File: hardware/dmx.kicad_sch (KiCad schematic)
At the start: 38 parts, among them J101 Cortex, J102 DX07S016JA3, SW101 SKSG, SW102 SKSG, U101 TPS78433QWDRBRQ1, U102 ATSAMD51G, Y101 32k768

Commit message: Update Library
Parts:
- C101: symbol V2_Device:C_0603_10u -> V2_Capacitor:0603_10u
- C102, C103, C104, C105: symbol V2_Device:C_0603_0u1 -> V2_Capacitor:0603_0u1
- C106, C107: symbol V2_Device:C_0805_10u -> V2_Capacitor:0805_10u
- C108, C109: symbol V2_Device:C_0603_18p -> V2_Capacitor:0603_18p
- D103: symbol V2_Device:LED_0603_Orange -> V2_LED:0603_Orange
- INFO102: value (none) -> ~
- R101: symbol V2_Device:R_0603_330R -> V2_Resistor:0603_330R
- R102, R103: symbol V2_Device:R_0603_5k1 -> V2_Resistor:0603_5k1
- R104: symbol V2_Device:R_0603_100k -> V2_Resistor:0603_100k
- Y101: symbol V2_Device:Crystal_3.2x1.5_32k768 -> V2_Crystal:3.2x1.5_32k768

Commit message: Export stencil
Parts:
- INFO102: value ~ -> (none)
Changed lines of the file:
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@@
 	(title_block
 		(title "V2 dmx")
-		(date "2026-02-10")
+		(date "2026-02-25")
 		(rev "2026-01-06")
 		(company "Versio Duo")
@@
 			)
 		)
-		(property "Value" "~"
+		(property "Value" ""
 			(at 181.61 194.31 0)
 			(effects

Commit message: Refresh
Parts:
- C108, C109: Manufacturer YAGEO -> TDK; Mouser 603-CC603JRNPO9BN180 -> 810-CGA3E2C0G1H180J; Product CC0603JRNPO9BN180 -> CGA3E2C0G1H180J080AA
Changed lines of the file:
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@@
 	(title_block
 		(title "V2 dmx")
-		(date "2026-02-25")
+		(date "2026-03-11")
 		(rev "2026-01-06")
 		(company "Versio Duo")
@@
 			)
 		)
-		(property "Description" "Resistor, small symbol"
+		(property "Description" ""
 			(at 228.092 96.52 0)
 			(effects
@@
 			)
 		)
-		(property "Description" "Unpolarized capacitor, small symbol"
+		(property "Description" ""
 			(at 115.57 37.592 0)
 			(effects
@@
 			)
 		)
-		(property "Description" "Push button switch, generic, two pins"
+		(property "Description" "Push button"
 			(at 254 35.052 0)
 			(effects
@@
 			)
 		)
-		(property "Description" "Light emitting diode, small symbol"
+		(property "Description" ""
 			(at 129.54 51.308 0)
 			(effects
@@
 			)
 		)
-		(property "Description" "Unpolarized capacitor, small symbol"
+		(property "Description" ""
 			(at 205.74 55.372 0)
 			(effects
@@
 			)
 		)
-		(property "Description" "Unpolarized capacitor, small symbol"
+		(property "Description" ""
 			(at 180.34 55.372 0)
 			(effects
@@
 			)
 		)
-		(property "Description" "Two pin crystal, small symbol"
+		(property "Description" ""
 			(at 34.29 51.054 0)
 			(effects
@@
 			)
 		)
-		(property "Description" "Unpolarized capacitor, small symbol"
+		(property "Description" ""
 			(at 36.83 60.452 0)
 			(effects
@@
 			)
 		)
-		(property "Mouser" "603-CC603JRNPO9BN180"
+		(property "Mouser" "810-CGA3E2C0G1H180J"
 			(at 36.83 67.31 0)
 			(effects
@@
 			)
 		)
-		(property "Product" "CC0603JRNPO9BN180"
+		(property "Product" "CGA3E2C0G1H180J080AA"
 			(at 36.83 67.564 0)
 			(effects
@@
 			)
 		)
-		(property "Manufacturer" "YAGEO"
+		(property "Manufacturer" "TDK"
 			(at 36.83 64.77 0)
 			(effects
@@
 			)
 		)
-		(property "Description" "Unpolarized capacitor, small symbol"
+		(property "Description" ""
 			(at 63.5 37.592 0)
 			(effects
@@
 			)
 		)
-		(property "Description" "Unpolarized capacitor, small symbol"
+		(property "Description" ""
 			(at 31.75 60.452 0)
 			(effects
@@
 			)
 		)
-		(property "Mouser" "603-CC603JRNPO9BN180"
+		(property "Mouser" "810-CGA3E2C0G1H180J"
 			(at 31.75 67.31 0)
 			(effects
@@
 			)
 		)
-		(property "Product" "CC0603JRNPO9BN180"
+		(property "Product" "CGA3E2C0G1H180J080AA"
 			(at 31.75 67.564 0)
 			(effects
@@
 			)
 		)
-		(property "Manufacturer" "YAGEO"
+		(property "Manufacturer" "TDK"
 			(at 31.75 64.77 0)
 			(effects
@@
 			)
 		)
-		(property "Description" "Resistor, small symbol"
+		(property "Description" ""
 			(at 150.622 58.42 0)
 			(effects
@@
 			)
 		)
-		(property "Description" "Unpolarized capacitor, small symbol"
+		(property "Description" ""
 			(at 105.41 37.592 0)
 			(effects
@@
 			)
 		)
-		(property "Description" "Unpolarized capacitor, small symbol"
+		(property "Description" ""
 			(at 85.09 37.592 0)
 			(effects
@@
 			)
 		)
-		(property "Description" "Resistor, small symbol"
+		(property "Description" ""
 			(at 228.092 99.06 0)
 			(effects
@@
 			)
 		)
-		(property "Description" "Push button switch, generic, two pins"
+		(property "Description" "Push button"
 			(at 129.54 82.042 0)
 			(effects
@@
 			)
 		)
-		(property "Description" "Unpolarized capacitor, small symbol"
+		(property "Description" ""
 			(at 95.25 37.592 0)
 			(effects
@@
 			)
 		)
-		(property "Description" "Resistor, small symbol"
+		(property "Description" ""
 			(at 69.342 121.92 0)
 			(effects

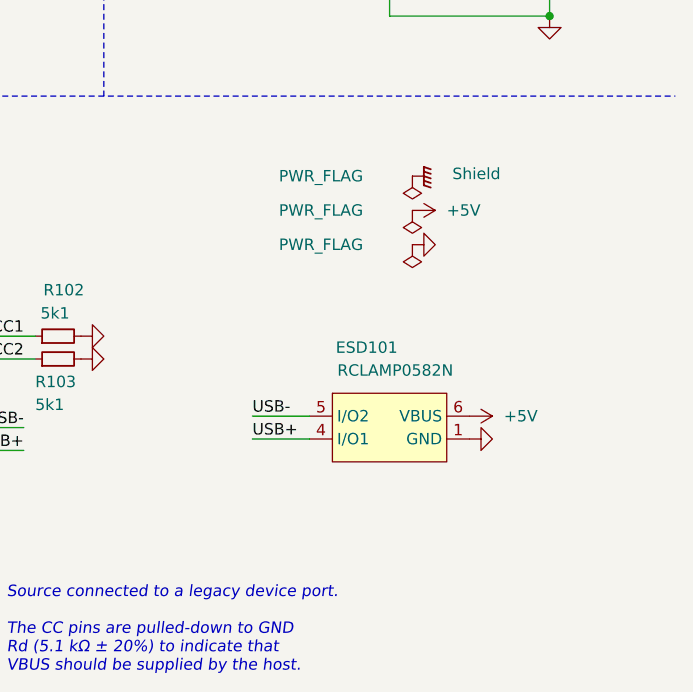
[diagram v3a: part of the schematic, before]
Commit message: Update ESD suppressor
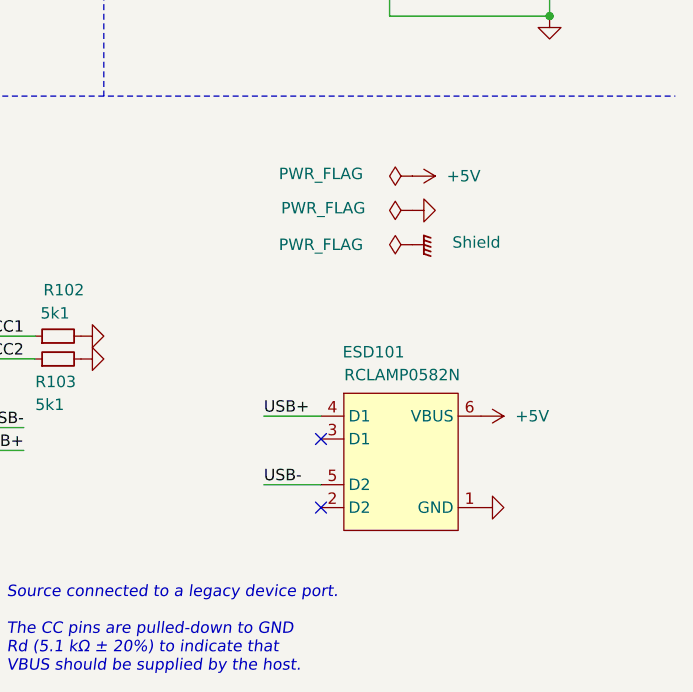
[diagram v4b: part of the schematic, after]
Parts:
- INFO102: value (none) -> ~
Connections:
- no-connect marks 27 -> 29

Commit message: Replace diode
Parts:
- INFO102: value ~ -> (none)

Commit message: Update
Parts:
- C101, C102, C103, C104, C105, C106, C107: Id (none) -> Capacitor:${SYMBOL_NAME}
- C108, C109: Id (none) -> Capacitor:${SYMBOL_NAME}; Rating (none) -> 50V
- D101, D102: Id (none) -> LED:${SYMBOL_NAME}; Rating (none) -> 15mA
- D103: Id (none) -> LED:${SYMBOL_NAME}; Rating (none) -> 605nm
- ESD101: Id (none) -> ESD:${SYMBOL_NAME}; Rating (none) -> 20kV
- J102: Id (none) -> USB:${SYMBOL_NAME}; Rating (none) -> USB2.0
- R101, R102, R103, R104: Id (none) -> Resistor:${SYMBOL_NAME}
- SW101, SW102: Id (none) -> Button:${SYMBOL_NAME}; Rating (none) -> 1.6N
- U101: Id (none) -> LDO:${SYMBOL_NAME}; Rating (none) -> 300mA
- U102: Id (none) -> MCU:${SYMBOL_NAME}; Rating (none) -> Cortex-M4F
- Y101: Id (none) -> Crystal:${SYMBOL_NAME}; Rating (none) -> 10ppm

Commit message: Update
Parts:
- renumbered C108 to C101, C109 to C102, C101 to C103, C102 to C104, C103 to C105, C104 to C106, C105 to C107, C106 to C108, C107 to C109, D103 to D101, D101 to D102, D102 to D103, ICON104 to ICON101, ICON101 to ICON103, ICON103 to ICON104, INFO102 to INFO101, INFO101 to INFO102, R104 to R101, R101 to R102, R102 to R103, R103 to R104, SW102 to SW101, SW101 to SW102, U102 to U101, U101 to U102

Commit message: Good Bye Imperial
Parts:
- C101, C102: footprint V2_Capacitor_SMD:C_0603 -> V2_Capacitor_SMD:C_1608; symbol V2_Capacitor:0603_18p -> V2_Capacitor:1608_18p
- C103: footprint V2_Capacitor_SMD:C_0603 -> V2_Capacitor_SMD:C_1608; symbol V2_Capacitor:0603_10u -> V2_Capacitor:1608_10u
- C104, C105, C106, C107: footprint V2_Capacitor_SMD:C_0603 -> V2_Capacitor_SMD:C_1608; symbol V2_Capacitor:0603_0u1 -> V2_Capacitor:1608_0u1
- C108, C109: footprint V2_Capacitor_SMD:C_0805 -> V2_Capacitor_SMD:C_2012; symbol V2_Capacitor:0805_10u -> V2_Capacitor:2012_10u
- D101: footprint V2_LED:LED_0603 -> V2_LED:LED_1608; symbol V2_LED:0603_Orange -> V2_LED:1608_Orange
- R101: footprint V2_Resistor_SMD:R_0603 -> V2_Resistor_SMD:R_1608; symbol V2_Resistor:0603_100k -> V2_Resistor:1608_100k
- R102: footprint V2_Resistor_SMD:R_0603 -> V2_Resistor_SMD:R_1608; symbol V2_Resistor:0603_330R -> V2_Resistor:1608_330R
- R103, R104: footprint V2_Resistor_SMD:R_0603 -> V2_Resistor_SMD:R_1608; symbol V2_Resistor:0603_5k1 -> V2_Resistor:1608_5k1
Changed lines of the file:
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@@
 	(title_block
 		(title "V2 dmx")
-		(date "2026-04-14")
+		(date "2026-05-11")
 		(rev "2026-03-30")
 		(company "Versio Duo")
@@
 	)
 	(symbol
-		(lib_id "V2_Resistor:0603_5k1")
+		(lib_id "V2_Resistor:1608_5k1")
 		(at 215.9 96.52 90)
 		(unit 1)
@@
 			)
 		)
-		(property "Footprint" "V2_Resistor_SMD:R_0603"
+		(property "Footprint" "V2_Resistor_SMD:R_1608"
 			(at 231.648 96.52 0)
 			(hide yes)
@@
 	)
 	(symbol
-		(lib_id "V2_Capacitor:0603_0u1")
+		(lib_id "V2_Capacitor:1608_0u1")
 		(at 115.57 24.13 0)
 		(unit 1)
@@
 			)
 		)
-		(property "Footprint" "V2_Capacitor_SMD:C_0603"
+		(property "Footprint" "V2_Capacitor_SMD:C_1608"
 			(at 115.57 41.148 0)
 			(hide yes)
@@
 	)
 	(symbol
-		(lib_id "V2_LED:0603_Orange")
+		(lib_id "V2_LED:1608_Orange")
 		(at 129.54 58.42 180)
 		(unit 1)
@@
 			)
 		)
-		(property "Footprint" "V2_LED:LED_0603"
+		(property "Footprint" "V2_LED:LED_1608"
 			(at 129.54 48.514 0)
 			(hide yes)
@@
 	)
 	(symbol
-		(lib_id "V2_Capacitor:0805_10u")
+		(lib_id "V2_Capacitor:2012_10u")
 		(at 205.74 41.91 0)
 		(unit 1)
@@
 			)
 		)
-		(property "Footprint" "V2_Capacitor_SMD:C_0805"
+		(property "Footprint" "V2_Capacitor_SMD:C_2012"
 			(at 205.74 58.928 0)
 			(hide yes)
@@
 	)
 	(symbol
-		(lib_id "V2_Capacitor:0805_10u")
+		(lib_id "V2_Capacitor:2012_10u")
 		(at 180.34 41.91 0)
 		(unit 1)
@@
 			)
 		)
-		(property "Footprint" "V2_Capacitor_SMD:C_0805"
+		(property "Footprint" "V2_Capacitor_SMD:C_2012"
 			(at 180.34 58.928 0)
 			(hide yes)
@@
 	)
 	(symbol
-		(lib_id "V2_Capacitor:0603_18p")
+		(lib_id "V2_Capacitor:1608_18p")
 		(at 36.83 46.99 0)
 		(unit 1)
@@
 			)
 		)
-		(property "Footprint" "V2_Capacitor_SMD:C_0603"
+		(property "Footprint" "V2_Capacitor_SMD:C_1608"
 			(at 36.83 64.008 0)
 			(hide yes)
@@
 	)
 	(symbol
-		(lib_id "V2_Capacitor:0603_10u")
+		(lib_id "V2_Capacitor:1608_10u")
 		(at 63.5 24.13 0)
 		(unit 1)
@@
 			)
 		)
-		(property "Footprint" "V2_Capacitor_SMD:C_0603"
+		(property "Footprint" "V2_Capacitor_SMD:C_1608"
 			(at 63.5 41.148 0)
 			(hide yes)
@@
 	)
 	(symbol
-		(lib_id "V2_Capacitor:0603_18p")
+		(lib_id "V2_Capacitor:1608_18p")
 		(at 31.75 46.99 0)
 		(unit 1)
@@
 			)
 		)
-		(property "Footprint" "V2_Capacitor_SMD:C_0603"
+		(property "Footprint" "V2_Capacitor_SMD:C_1608"
 			(at 31.75 64.008 0)
 			(hide yes)
@@
 	)
 	(symbol
-		(lib_id "V2_Resistor:0603_330R")
+		(lib_id "V2_Resistor:1608_330R")
 		(at 138.43 58.42 90)
 		(unit 1)
@@
 			)
 		)
-		(property "Footprint" "V2_Resistor_SMD:R_0603"
+		(property "Footprint" "V2_Resistor_SMD:R_1608"
 			(at 154.178 58.42 0)
 			(hide yes)
@@
 	)
 	(symbol
-		(lib_id "V2_Capacitor:0603_0u1")
+		(lib_id "V2_Capacitor:1608_0u1")
 		(at 105.41 24.13 0)
 		(unit 1)
@@
 			)
 		)
-		(property "Footprint" "V2_Capacitor_SMD:C_0603"
+		(property "Footprint" "V2_Capacitor_SMD:C_1608"
 			(at 105.41 41.148 0)
 			(hide yes)
@@
 	)
 	(symbol
-		(lib_id "V2_Capacitor:0603_0u1")
+		(lib_id "V2_Capacitor:1608_0u1")
 		(at 85.09 24.13 0)
 		(unit 1)
@@
 			)
 		)
-		(property "Footprint" "V2_Capacitor_SMD:C_0603"
+		(property "Footprint" "V2_Capacitor_SMD:C_1608"
 			(at 85.09 41.148 0)
 			(hide yes)
@@
 	)
 	(symbol
-		(lib_id "V2_Resistor:0603_5k1")
+		(lib_id "V2_Resistor:1608_5k1")
 		(at 215.9 99.06 90)
 		(unit 1)
@@
 			)
 		)
-		(property "Footprint" "V2_Resistor_SMD:R_0603"
+		(property "Footprint" "V2_Resistor_SMD:R_1608"
 			(at 231.648 99.06 0)
 			(hide yes)
@@
 	)
 	(symbol
-		(lib_id "V2_Capacitor:0603_0u1")
+		(lib_id "V2_Capacitor:1608_0u1")
 		(at 95.25 24.13 0)
 		(unit 1)
@@
 			)
 		)
-		(property "Footprint" "V2_Capacitor_SMD:C_0603"
+		(property "Footprint" "V2_Capacitor_SMD:C_1608"
 			(at 95.25 41.148 0)
 			(hide yes)
@@
 	)
 	(symbol
-		(lib_id "V2_Resistor:0603_100k")
+		(lib_id "V2_Resistor:1608_100k")
 		(at 57.15 121.92 90)
 		(unit 1)
@@
 			)
 		)
-		(property "Footprint" "V2_Resistor_SMD:R_0603"
+		(property "Footprint" "V2_Resistor_SMD:R_1608"
 			(at 72.898 121.92 0)
 			(hide yes)
